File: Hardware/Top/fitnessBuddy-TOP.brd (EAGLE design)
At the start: 38 x 38 mm, 50 parts, among them SW3 SWITCH.MOM, SW4 SWITCH.MOM, U1 NRF52832_MODULE_MDBT42, U2 FT231XS

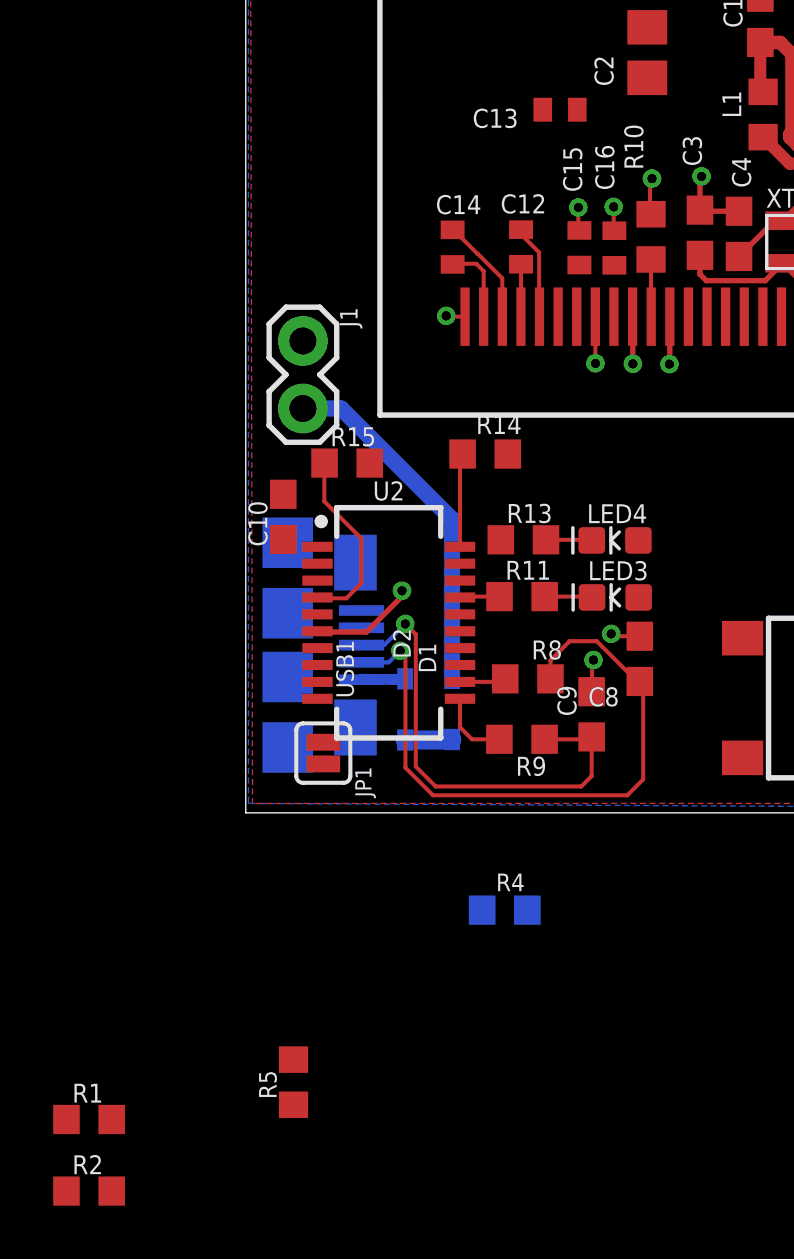
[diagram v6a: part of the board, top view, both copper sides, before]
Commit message: finished routing power management on top board
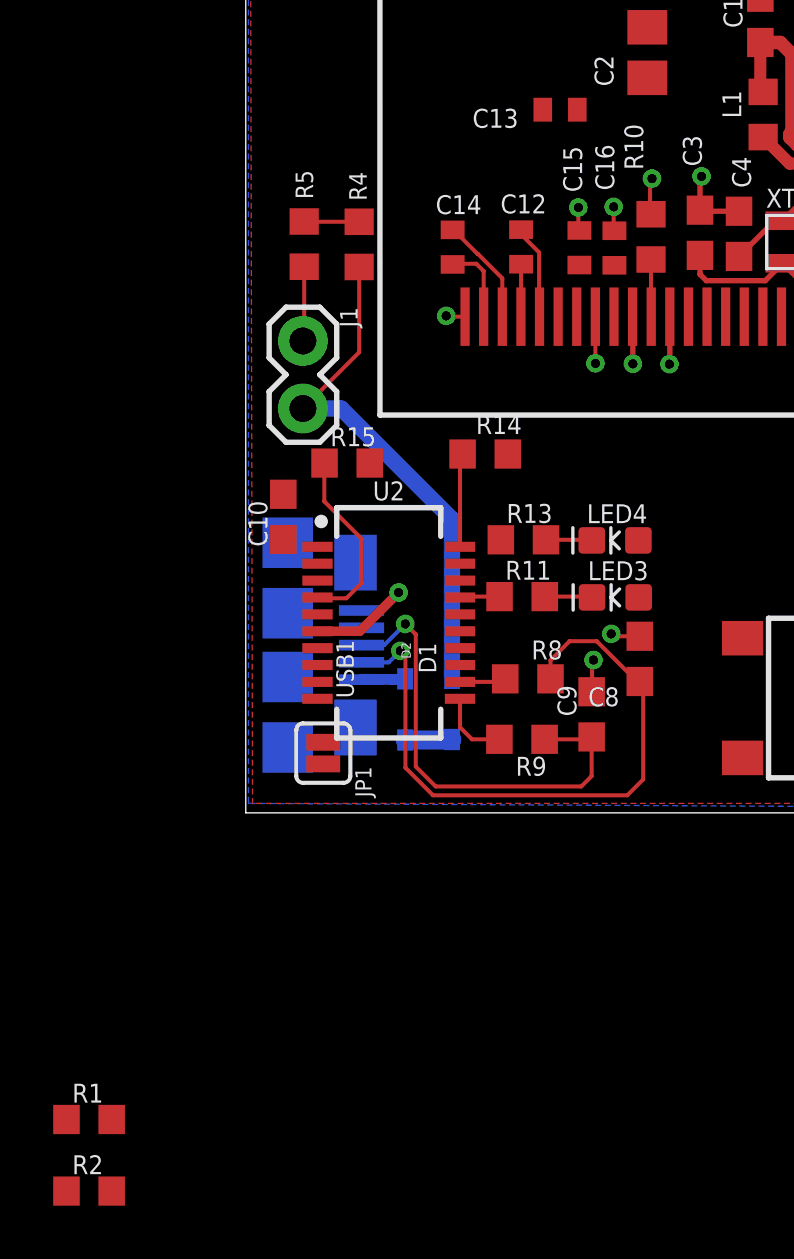
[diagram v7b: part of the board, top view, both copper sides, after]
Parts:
- moved R5 31.5 mm to (2.20, 21.4)
- moved R4 25.6 mm to (4.26, 21.4), flipped to the top, turned to 270 degrees
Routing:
- net VLIPO: track 13.3 -> 19.5 mm
- net GND: track 35.3 -> 37.9 mm
- net A4/BATT: track 0.00 -> 2.07 mm
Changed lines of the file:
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@@
 </element>
 <element name="D2" library="LinnesLab-DiscreteSemi" package="USC" package3d_urn="urn:adsk.eagle:package:15664784/2" value="" x="5.9918625" y="3.891278125" smashed="yes" rot="MR270">
-<attribute name="NAME" x="6.20758125" y="5.79881875" size="0.6604" layer="25" rot="R90"/>
+<attribute name="NAME" x="6.20758125" y="5.79881875" size="0.3556" layer="25" rot="R90"/>
 <attribute name="VALUE" x="7.6568625" y="5.161278125" size="0.635" layer="28" rot="MR270"/>
 </element>
@@
 <attribute name="VALUE" x="0.11684375" y="19.016978125" size="0.6096" layer="27" font="vector" ratio="20" rot="R270"/>
 </element>
-<element name="R4" library="LinnesLab-Passives" package="R0603" package3d_urn="urn:adsk.eagle:package:15661944/2" value="100k" x="9.738359375" y="-3.657596875" smashed="yes" rot="MR0">
-<attribute name="NAME" x="9.4107" y="-2.94385625" size="0.6604" layer="25"/>
-<attribute name="VALUE" x="10.373359375" y="-5.562596875" size="1.27" layer="28" rot="MR0"/>
-</element>
-<element name="R5" library="LinnesLab-Passives" package="R0603" package3d_urn="urn:adsk.eagle:package:15661944/2" value="100k" x="1.79578125" y="-10.12951875" smashed="yes" rot="R90">
-<attribute name="NAME" x="1.16078125" y="-10.76451875" size="0.6604" layer="25" rot="R90"/>
-<attribute name="VALUE" x="3.70078125" y="-10.76451875" size="1.27" layer="27" rot="R90"/>
+<element name="R4" library="LinnesLab-Passives" package="R0603" package3d_urn="urn:adsk.eagle:package:15661944/2" value="100k" x="4.264665625" y="21.379178125" smashed="yes" rot="R270">
+<attribute name="NAME" x="4.54914375" y="23.02001875" size="0.6604" layer="25" rot="R90"/>
+<attribute name="VALUE" x="2.359665625" y="22.014178125" size="1.27" layer="27" rot="R270"/>
+</element>
+<element name="R5" library="LinnesLab-Passives" package="R0603" package3d_urn="urn:adsk.eagle:package:15661944/2" value="100k" x="2.1971" y="21.38934375" smashed="yes" rot="R90">
+<attribute name="NAME" x="2.53238125" y="23.083521875" size="0.6604" layer="25" rot="R90"/>
+<attribute name="VALUE" x="4.1021" y="20.75434375" size="1.27" layer="27" rot="R90"/>
 </element>
 <element name="USB1" library="LinnesLab-Connectors" package="USB-MICRO-01.BIGGERPADS" value="USB.MICRO-BIGGERPADS" x="2.847340625" y="6.309359375" smashed="yes" rot="MR90">
@@
 <via x="26.692859375" y="3.66268125" extent="1-16" drill="0.35"/>
 <wire x1="2.697478125" y1="6.83005625" x2="2.72795625" y2="6.799578125" width="0.2032" layer="1"/>
-<wire x1="4.533896875" y1="6.799578125" x2="2.72795625" y2="6.799578125" width="0.2032" layer="1"/>
-<wire x1="5.87501875" y1="8.1407" x2="5.87501875" y2="8.354059375" width="0.2032" layer="1"/>
-<wire x1="5.87501875" y1="8.1407" x2="4.533896875" y2="6.799578125" width="0.2032" layer="1"/>
-<via x="5.87501875" y="8.354059375" extent="1-16" drill="0.35"/>
 <wire x1="18.54961875" y1="22.6254125" x2="17.122140625" y2="22.6254125" width="0.2032" layer="1"/>
 <wire x1="17.122140625" y1="22.6254125" x2="17.081496875" y2="22.66605625" width="0.2032" layer="1"/>
@@
 <wire x1="13.835553125" y1="6.641190625" x2="13.74484375" y2="6.7319" width="0.1524" layer="1"/>
 <via x="13.74484375" y="6.7319" extent="1-16" drill="0.35"/>
+<wire x1="2.697478125" y1="6.83005625" x2="4.29005625" y2="6.83005625" width="0.3556" layer="1"/>
+<wire x1="4.29005625" y1="6.83005625" x2="5.74801875" y2="8.28801875" width="0.3556" layer="1"/>
+<via x="5.74801875" y="8.28801875" extent="1-16" drill="0.35"/>
+<wire x1="2.1971" y1="20.53934375" x2="2.1971" y2="17.795234375" width="0.1524" layer="1"/>
+<wire x1="2.1971" y1="17.795234375" x2="2.14884375" y2="17.746978125" width="0.1524" layer="1"/>
 <wire x1="31.036321875" y1="33.01761875" x2="33.949840625" y2="36.496759375" width="0" layer="19" extent="1-1"/>
 <wire x1="34.6329" y1="30.0482" x2="31.036321875" y2="33.01761875" width="0" layer="19" extent="1-1"/>
@@
 <wire x1="4.127340625" y1="9.409359375" x2="1.577340625" y2="10.159359375" width="0" layer="19" extent="16-16"/>
 <wire x1="4.352340625" y1="7.609359375" x2="4.127340625" y2="9.409359375" width="0" layer="19" extent="16-16"/>
-<wire x1="5.87501875" y1="8.354059375" x2="4.352340625" y2="7.609359375" width="0" layer="19" extent="16-16"/>
+<wire x1="5.74801875" y1="8.28801875" x2="4.352340625" y2="7.609359375" width="0" layer="19" extent="16-16"/>
 <wire x1="1.577340625" y1="7.509359375" x2="2.697478125" y2="6.83005625" width="0" layer="19" extent="1-16"/>
-<wire x1="1.577340625" y1="5.109359375" x2="2.697478125" y2="6.83005625" width="0" layer="19" extent="1-16"/>
-<wire x1="8.056878125" y1="7.46505625" x2="5.87501875" y2="8.354059375" width="0" layer="19" extent="1-1"/>
+<wire x1="1.577340625" y1="5.109359375" x2="2.72795625" y2="6.799578125" width="0" layer="19" extent="1-16"/>
+<wire x1="8.056878125" y1="7.46505625" x2="5.74801875" y2="8.28801875" width="0" layer="19" extent="1-1"/>
 <wire x1="1.577340625" y1="2.459359375" x2="1.577340625" y2="5.109359375" width="0" layer="19" extent="16-16"/>
 <wire x1="2.91591875" y1="1.8415" x2="1.577340625" y2="2.459359375" width="0" layer="19" extent="1-16"/>
@@
 <wire x1="28.64114375" y1="2.01211875" x2="26.634340625" y2="2.068003125" width="0" layer="19" extent="1-1"/>
 <wire x1="36.59114375" y1="2.01211875" x2="28.64114375" y2="2.01211875" width="0" layer="19" extent="1-1"/>
-<wire x1="1.79578125" y1="-10.97951875" x2="2.91591875" y2="1.8415" width="0" layer="19" extent="1-1"/>
 </signal>
 <signal name="N$4">
@@
 <wire x1="7.75461875" y1="5.059065625" x2="7.75461875" y2="11.03884375" width="0.6096" layer="16"/>
 <wire x1="7.75461875" y1="11.03884375" x2="3.586484375" y2="15.206978125" width="0.6096" layer="16"/>
-<wire x1="7.75461875" y1="5.059065625" x2="8.888359375" y2="-3.657596875" width="0" layer="19" extent="16-16"/>
+<wire x1="4.264665625" y1="20.529178125" x2="4.264665625" y2="17.3228" width="0.1524" layer="1"/>
+<wire x1="4.264665625" y1="17.3228" x2="2.14884375" y2="15.206978125" width="0.1524" layer="1"/>
 </signal>
 <signal name="V_USB">
@@
 <contactref element="R4" pad="1"/>
 <contactref element="R5" pad="2"/>
-<wire x1="10.588359375" y1="-3.657596875" x2="21.836321875" y2="27.91761875" width="0" layer="19" extent="1-16"/>
-<wire x1="1.79578125" y1="-9.27951875" x2="10.588359375" y2="-3.657596875" width="0" layer="19" extent="1-16"/>
+<wire x1="4.264665625" y1="22.229178125" x2="2.207265625" y2="22.229178125" width="0.1524" layer="1"/>
+<wire x1="2.207265625" y1="22.229178125" x2="2.1971" y2="22.23934375" width="0.1524" layer="1"/>
+<wire x1="4.264665625" y1="22.229178125" x2="21.836321875" y2="27.91761875" width="0" layer="19" extent="1-1"/>
 </signal>
 <signal name="D7/SD.CS">

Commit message: finished halfway through take 007. organized board/ connected airwires
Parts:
- C13: device LinnesLab-Passives:C0402 -> LinnesLab-Passives:C0603
- moved R2 46.1 mm to (2.91, 31.0), turned to 270 degrees
- moved R1 43.1 mm to (1.34, 31.0), turned to 270 degrees
- moved C13 21.7 mm to (29.7, 14.1), turned to 180 degrees
- moved R15 16.3 mm to (20.0, 10.6)
- moved R14 11.9 mm to (19.9, 8.80)
- moved SW3 11.3 mm to (21.3, 4.02)
- moved SW4 9.13 mm to (31.8, 4.06)
- moved C2 3.74 mm to (18.0, 31.0), turned to 0 degrees
- moved C10 2.68 mm to (3.63, 12.6), turned to 180 degrees
- moved L1 1.81 mm to (18.5, 27.8), turned to 0 degrees
- moved JP1 1.33 mm to (1.60, 2.36)
- moved C4 1.25 mm to (18.5, 23.0)
- moved C3 1.23 mm to (17.2, 23.0)
- moved SW2 1.14 mm to (35.5, 14.9), turned to 90 degrees
- moved D3 1.11 mm to (35.3, 10.2)
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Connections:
- removed net !DTR: U2.1
- removed net A4/BATT: R4.1, R5.2, U1.5
- removed net A6/TIA: J2.6, U1.7
- removed net A7/PPG: J2.7, U1.8
- removed net D29/LED.CTRL: J2.5, U1.6
- new net A4/PPG: J2.7, U1.5
- new net A5/TIA: J2.6, U1.6
- new net A7/BATT: R4.1, R5.2, U1.8
- new net D30/LED.CTRL: J2.5, U1.7
- net DTR: now also U2.1
- net GND: no longer SW3.B2, SW4.B2
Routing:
- net DTR: track 0.00 -> 42.0 mm, vias 0 -> 2
- net SDA: track 0.00 -> 25.0 mm, vias 0 -> 1
- net SCL: track 0.00 -> 24.9 mm, vias 0 -> 1
- net RXD.NRF: track 0.00 -> 24.9 mm, vias 0 -> 2
- net D15/SW2: track 0.76 -> 25.3 mm, vias 0 -> 2
- net A7/BATT: track 0.00 -> 23.3 mm, vias 0 -> 2
- net MOSI: track 0.00 -> 20.4 mm, vias 0 -> 2
- net D11/SW1: track 0.03 -> 20.3 mm
- net TXD.NRF: track 0.00 -> 19.8 mm, vias 0 -> 2
- net D16/CS.OLED: track 0.00 -> 18.8 mm, vias 0 -> 2
- net SCK: track 0.00 -> 15.9 mm, vias 0 -> 2
- net GND: track 37.9 -> 53.7 mm, vias 19 -> 25
- net D30/LED.CTRL: track 0.00 -> 14.5 mm, vias 0 -> 1
- net D3/RESET.OLED: track 0.00 -> 13.9 mm, vias 0 -> 2
- net D4/DC.OLED: track 0.00 -> 13.6 mm, vias 0 -> 2
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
